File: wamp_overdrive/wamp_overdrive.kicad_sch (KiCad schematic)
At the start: 21 parts, among them J1 AudioJack2, J2 AudioJack2, U1 TL082

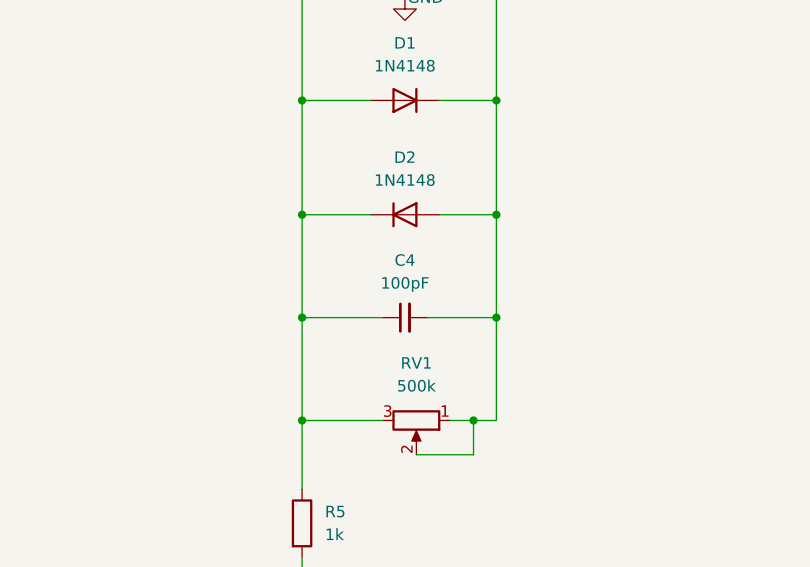
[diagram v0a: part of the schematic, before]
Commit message: updated the wampler overdrive pedal schematic
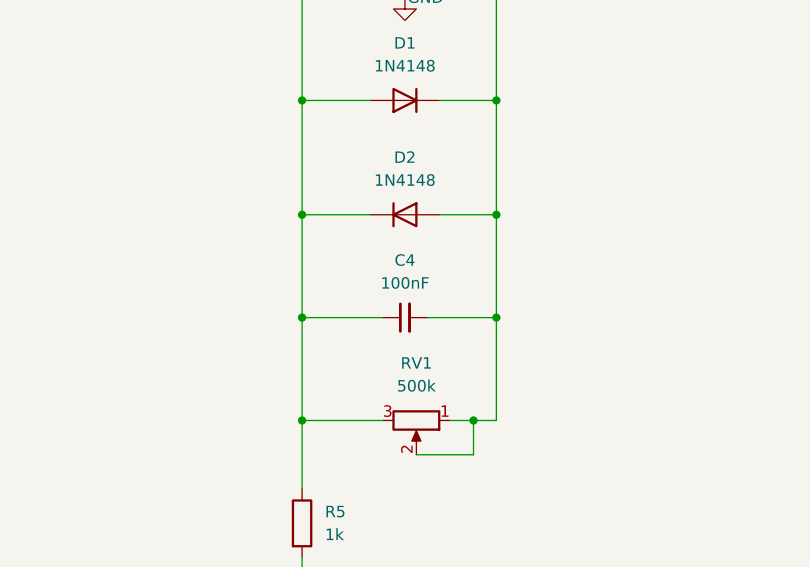
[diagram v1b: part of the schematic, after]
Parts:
- C4: value 100pF -> 100nF
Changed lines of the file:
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@@
 			)
 		)
-		(property "Value" "100pF"
+		(property "Value" "100nF"
 			(at 138.4363 120.65 90)
 			(effects
